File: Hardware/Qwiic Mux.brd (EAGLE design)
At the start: 40.6 x 54.6 mm, 78 parts, among them J1 SMD, J10 SMD, J11 PTH, J12 PTH, J13 PTH, J14 PTH, J2 SMD, J23 SMD, J24 SMD, J25 SMD, J26 SMD, J3 PTH, J4 PTH, J5 PTH, J6 PTH, J7 PTH, J8 SMD, J9 SMD, U2 PCA9548A, U3 3.3V/150mA, U4 2.8V/150mA

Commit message: Post design Review Changes
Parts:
- removed C10, C11, C13: 10uF, SparkFun-Capacitors:0603
- removed C12: 1.0uF, SparkFun-Capacitors:0603
- removed D1: GREEN, SparkFun-LED:LED-0603
- removed D4: BLUE, SparkFun-LED:LED-0603
- removed J11, J12, J13, J14, J3, J4, J5, J6, J7: PTH, SparkX:1X04_NO_SILK
- removed JP5: (no value), SparkFun-Jumpers:SMT-JUMPER_3_1-NC_TRACE_SILK
- removed R23, R25: 330, SparkFun-Resistors:0603
- removed U3: 3.3V/150mA, SparkFun-IC-Power:SOT23-5
- removed U4: 2.8V/150mA, SparkFun-IC-Power:SOT23-5
- added FD3, FD4: FIDUCIAL1X2, SparkFun-Aesthetics:FIDUCIAL-1X2
- added JP4: JUMPER-SMT_3_2-NC_PASTE_NO-SILK, SparkFun-Jumpers:SMT-JUMPER_3_2-NC_PASTE_NO-SILK
- added U$3: (no value), Labels-0_04:(PWR)
- added U$4: (no value), Labels-0_04:(QWIIC)
- added U$5: (no value), Labels-0_04:(I2C)
- D2: value Yellow -> RED
- R24: value 330 -> 1k
- U2: device SparkX:TSSOP28 -> SparkFun-IC-Logic:TSSOP28
- moved FD2 5.08 mm to (30.5, 1.27)
- moved H3 5.08 mm to (33.0, 52.1)
- moved H4 5.08 mm to (33.0, 2.54)
- moved J23 5.08 mm to (30.5, 10.2)
- moved J24 5.08 mm to (30.5, 20.3)
- moved J25 5.08 mm to (30.5, 30.5)
- moved J26 5.08 mm to (30.5, 40.6)
- moved JP1 2.62 mm to (20.3, 37.5)
- moved JP2 2.62 mm to (17.8, 37.5)
- moved JP3 2.62 mm to (15.2, 37.5)
- moved C2 2.55 mm to (9.14, 39.1)
- moved C3 2.55 mm to (9.14, 29.0)
- moved C4 2.55 mm to (9.14, 18.8)
- moved C5 2.55 mm to (9.14, 8.64)
- moved C6 2.55 mm to (26.4, 8.64)
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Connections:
- removed net 2.8V: C13.1, C4.1, C7.1, D1.A, J12.2, J24.2, J6.2, J9.2, R10.1, R13.1, R14.1, R9.1, U4.5
- removed net 5V: C10.1, C5.1, C6.1, D4.A, J10.2, J11.2, J23.2, J7.2, JP5.1, R11.1, R12.1, R2.1, R3.1, U3.1, U3.3
- removed net N$4: D4.C, R23.2
- removed net VIN: J2.2, J3.2, JP5.2
- new net N$2: JP4.3, R4.1
- net 3.3V: now also C4.1, C5.1, C6.1, C7.1, J10.2, J2.2, J23.2, J24.2, J9.2, JP4.2, R10.1, R11.1, R12.1, R13.1, R14.1, R2.1, R3.1, R9.1; no longer C11.1, C12.1, J13.2, J14.2, J4.2, J5.2, JP5.3, R4.1, R5.1, U3.5, U4.1, U4.3
- net GND: no longer C10.2, C11.2, C12.2, C13.2, J11.1, J12.1, J13.1, J14.1, J3.1, J4.1, J5.1, J6.1, J7.1, R23.1, R25.1, U3.2, U4.2
- net MAIN_SCL: no longer J3.4
- net MAIN_SDA: no longer J3.3
- net N$3: now also JP4.1, R5.1; no longer D1.C, R25.2
- net SCL0: no longer J4.4
- net SCL1: no longer J5.4
- net SCL2: no longer J6.4
- net SCL3: no longer J7.4
- net SCL4: no longer J11.4
- net SCL5: no longer J12.4
- net SCL6: no longer J13.4
- net SCL7: no longer J14.4
- net SDA0: no longer J4.3
- net SDA1: no longer J5.3
- net SDA2: no longer J6.3
- net SDA3: no longer J7.3
- net SDA4: no longer J11.3
- net SDA5: no longer J12.3
- net SDA6: no longer J13.3
- net SDA7: no longer J14.3
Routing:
- net 5V: track 115.1 -> 0.00 mm, vias 3 -> 0
- net 2.8V: track 105.9 -> 0.00 mm, vias 3 -> 0
- net 3.3V: track 213.8 -> 256.0 mm, vias 4 -> 6
- net VIN: track 8.46 -> 0.00 mm
- net SCL2: track 19.3 -> 13.8 mm
- net SCL3: track 25.9 -> 20.5 mm
- net SCL4: track 23.9 -> 19.8 mm
- net SCL0: track 26.4 -> 22.5 mm
- net SDA4: track 23.8 -> 20.0 mm
- net SDA2: track 16.6 -> 12.9 mm
- net SDA5: track 15.8 -> 12.3 mm
- net SCL1: track 19.8 -> 16.4 mm
- net SDA0: track 27.6 -> 24.3 mm
- net SDA7: track 31.5 -> 28.2 mm
- net SDA6: track 22.6 -> 19.3 mm
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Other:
- board size 40.6 x 54.6 mm -> 35.6 x 54.6 mm
- board text added: "I C Mux"
- board text added: "Measures in Inches"
- board text removed: "2.8V"
- board text removed: "3.3V"
- board text removed: "5V"
- board text removed: "GND"
- board text removed: "Qwiic I C Mux"
- board text removed: "SCL"
- board text removed: "SCL0"
- board text removed: "SCL1"
- board text removed: "SCL2"
- board text removed: "SCL3"
- board text removed: "SCL4"
- board text removed: "SCL5"
- board text removed: "SCL6"
- board text removed: "SCL7"
- board text removed: "SDA"
- board text removed: "SDA0"
- board text removed: "SDA1"
- board text removed: "SDA2"
- board text removed: "SDA3"
- board text removed: "SDA4"
- board text removed: "SDA5"
- board text removed: "SDA6"
- board text removed: "SDA7"
- board text removed: "VIN"
- board text removed: "VIN SEL"

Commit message: checklist changes
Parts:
- added U$10, U$21: (no value), buzzard_labels (10):44
- added U$11, U$22: (no value), buzzard_labels (10):55
- added U$12, U$6: (no value), buzzard_labels (10):00
- added U$13, U$24: (no value), buzzard_labels (10):77
- added U$14, U$26: (no value), buzzard_labels (10):#RST10
- added U$15: (no value), buzzard_labels (10):I2C_MUX8
- added U$16, U$25: (no value), buzzard_labels (11):MAIN0
- added U$17, U$23: (no value), buzzard_labels (11):61
- added U$18, U$7: (no value), buzzard_labels (10):11
- added U$19, U$8: (no value), buzzard_labels (10):22
- added U$20, U$9: (no value), buzzard_labels (10):33
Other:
- board text added: "v10"
- board text removed: "!RST"
- board text removed: "3"
- board text removed: "4"
- board text removed: "5"
- board text removed: "6"
- board text removed: "7"
- board text removed: "I C Mux"
- board text removed: "Main"
- board text removed: "v01"

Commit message: Updated Qwiic connector
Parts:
- J1, J10, J23, J24, J25, J26, J8, J9: value SMD -> (none); device SparkX:1X04_1MM_RA -> SparkFun-Connectors:1X04_1MM_RA
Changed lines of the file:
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@@
 <layer number="59" name="tCarbon" color="7" fill="1" visible="no" active="no"/>
 <layer number="60" name="bCarbon" color="7" fill="1" visible="no" active="no"/>
+<layer number="88" name="SimResults" color="9" fill="1" visible="no" active="no"/>
+<layer number="89" name="SimProbes" color="9" fill="1" visible="no" active="no"/>
 <layer number="90" name="Modules" color="5" fill="1" visible="no" active="no"/>
 <layer number="91" name="Nets" color="2" fill="1" visible="no" active="no"/>
@@
 <element name="FD1" library="SparkFun-Aesthetics" package="FIDUCIAL-1X2" value="FIDUCIAL1X2" x="5.08" y="53.34" rot="R180"/>
 <element name="FD2" library="SparkFun-Aesthetics" package="FIDUCIAL-1X2" value="FIDUCIAL1X2" x="30.48" y="1.27" rot="R180"/>
-<element name="J1" library="SparkX" package="1X04_1MM_RA" value="SMD" x="5.08011875" y="40.63921875" smashed="yes" rot="R270">
+<element name="J1" library="SparkFun-Connectors" package="1X04_1MM_RA" value="" x="5.08011875" y="40.63921875" smashed="yes" rot="R270">
 <attribute name="NAME" x="2.92111875" y="42.03621875" size="0.6096" layer="25" font="vector" ratio="20" rot="R270"/>
-</element>
-<element name="J8" library="SparkX" package="1X04_1MM_RA" value="SMD" x="5.08011875" y="30.47921875" rot="R270"/>
-<element name="J9" library="SparkX" package="1X04_1MM_RA" value="SMD" x="5.08011875" y="20.31921875" rot="R270"/>
-<element name="J10" library="SparkX" package="1X04_1MM_RA" value="SMD" x="5.08011875" y="10.15921875" rot="R270"/>
+<attribute name="PROD_ID" value="CONN-13694" x="5.08011875" y="40.63921875" size="1.778" layer="27" rot="R270" display="off"/>
+<attribute name="VALUE" value="" x="5.08011875" y="40.63921875" size="1.778" layer="27" rot="R270" display="off"/>
+</element>
+<element name="J8" library="SparkFun-Connectors" package="1X04_1MM_RA" value="" x="5.08011875" y="30.47921875" rot="R270">
+<attribute name="PROD_ID" value="CONN-13694" x="5.08011875" y="30.47921875" size="1.778" layer="27" rot="R270" display="off"/>
+<attribute name="VALUE" value="" x="5.08011875" y="30.47921875" size="1.778" layer="27" rot="R270" display="off"/>
+</element>
+<element name="J9" library="SparkFun-Connectors" package="1X04_1MM_RA" value="" x="5.08011875" y="20.31921875" rot="R270">
+<attribute name="PROD_ID" value="CONN-13694" x="5.08011875" y="20.31921875" size="1.778" layer="27" rot="R270" display="off"/>
+<attribute name="VALUE" value="" x="5.08011875" y="20.31921875" size="1.778" layer="27" rot="R270" display="off"/>
+</element>
+<element name="J10" library="SparkFun-Connectors" package="1X04_1MM_RA" value="" x="5.08011875" y="10.15921875" rot="R270">
+<attribute name="PROD_ID" value="CONN-13694" x="5.08011875" y="10.15921875" size="1.778" layer="27" rot="R270" display="off"/>
+<attribute name="VALUE" value="" x="5.08011875" y="10.15921875" size="1.778" layer="27" rot="R270" display="off"/>
+</element>
 <element name="U$1" library="SparkFun-Aesthetics" package="SFE_LOGO_NAME_FLAME_.1" value="SFE_LOGO_NAME_FLAME.1_INCH" x="11.938" y="14.732"/>
 <element name="U$2" library="SparkFun-Aesthetics" package="SFE_LOGO_NAME_FLAME_.1" value="SFE_LOGO_NAME_FLAME.1_INCH" x="23.538" y="2.223" rot="MR0"/>
@@
 <attribute name="VALUE" value="4.7k" x="7.62011875" y="10.41321875" size="0.4064" layer="27" font="vector" rot="R180"/>
 </element>
-<element name="J23" library="SparkX" package="1X04_1MM_RA" value="SMD" x="30.47921875" y="10.15988125" rot="R90"/>
-<element name="J24" library="SparkX" package="1X04_1MM_RA" value="SMD" x="30.47921875" y="20.31988125" rot="R90"/>
-<element name="J25" library="SparkX" package="1X04_1MM_RA" value="SMD" x="30.47921875" y="30.47988125" rot="R90"/>
-<element name="J26" library="SparkX" package="1X04_1MM_RA" value="SMD" x="30.47921875" y="40.63988125" rot="R90"/>
+<element name="J23" library="SparkFun-Connectors" package="1X04_1MM_RA" value="" x="30.47921875" y="10.15988125" rot="R90">
+<attribute name="PROD_ID" value="CONN-13694" x="30.47921875" y="10.15988125" size="1.778" layer="27" rot="R90" display="off"/>
+<attribute name="VALUE" value="" x="30.47921875" y="10.15988125" size="1.778" layer="27" rot="R90" display="off"/>
+</element>
+<element name="J24" library="SparkFun-Connectors" package="1X04_1MM_RA" value="" x="30.47921875" y="20.31988125" rot="R90">
+<attribute name="PROD_ID" value="CONN-13694" x="30.47921875" y="20.31988125" size="1.778" layer="27" rot="R90" display="off"/>
+<attribute name="VALUE" value="" x="30.47921875" y="20.31988125" size="1.778" layer="27" rot="R90" display="off"/>
+</element>
+<element name="J25" library="SparkFun-Connectors" package="1X04_1MM_RA" value="" x="30.47921875" y="30.47988125" rot="R90">
+<attribute name="PROD_ID" value="CONN-13694" x="30.47921875" y="30.47988125" size="1.778" layer="27" rot="R90" display="off"/>
+<attribute name="VALUE" value="" x="30.47921875" y="30.47988125" size="1.778" layer="27" rot="R90" display="off"/>
+</element>
+<element name="J26" library="SparkFun-Connectors" package="1X04_1MM_RA" value="" x="30.47921875" y="40.63988125" rot="R90">
+<attribute name="PROD_ID" value="CONN-13694" x="30.47921875" y="40.63988125" size="1.778" layer="27" rot="R90" display="off"/>
+<attribute name="VALUE" value="" x="30.47921875" y="40.63988125" size="1.778" layer="27" rot="R90" display="off"/>
+</element>
 <element name="R2" library="SparkFun-Resistors" package="0603" value="4.7k" x="26.41588125" y="10.16078125">
 <attribute name="PROD_ID" value="RES-07857" x="-19.30411875" y="20.32078125" size="1.778" layer="27" font="vector" ratio="15" display="off"/>

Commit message: Update Board
Add second "Main" Qwiic connector
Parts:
- added J3: SMD, SparkX:1X04_1MM_RA
- added U$27, U$28: (no value), buzzard_labels (11):MAIN0
- moved U$3 45.2 mm to (23.4, 47.0)
- moved D2 44.4 mm to (25.9, 48.8), turned to 0 degrees
- moved R24 42.2 mm to (25.9, 50.3), turned to 0 degrees
- moved U$2 7.62 mm to (23.5, 9.84)
- moved U$15 2.16 mm to (11.9, 14.0)
- moved U$4 1.91 mm to (14.9, 15.9)
- moved U$1 1.27 mm to (11.9, 16.0)
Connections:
- net 3.3V: now also J3.2
- net GND: now also J3.1
- net MAIN_SCL: now also J3.4
- net MAIN_SDA: now also J3.3
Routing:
- net MAIN_SDA: track 32.0 -> 55.2 mm, vias 2 -> 3
- net MAIN_SCL: track 34.5 -> 56.9 mm
- net 3.3V: track 256.0 -> 267.6 mm
- net N$1: track 2.08 -> 1.54 mm
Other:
- board text added: "v1.1"
- board text removed: "v10"

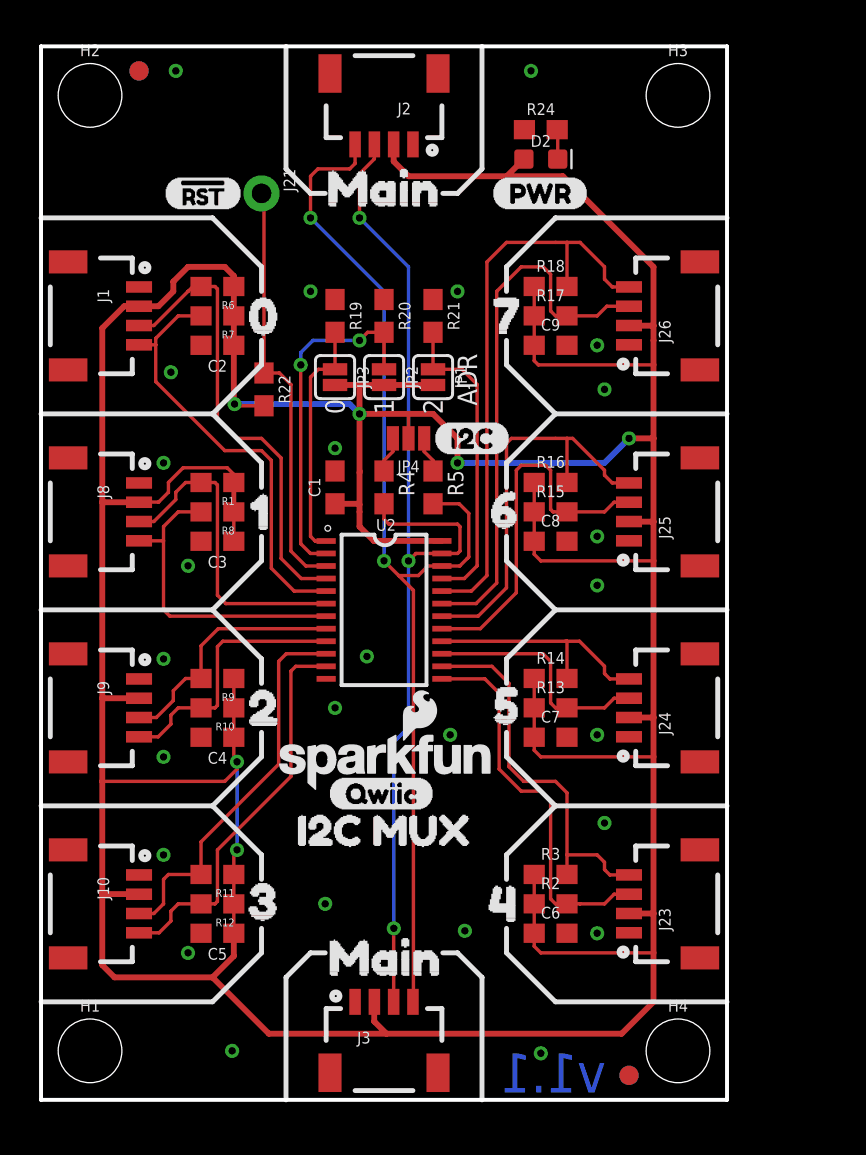
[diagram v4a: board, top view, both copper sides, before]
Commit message: Fix routing and version numbering
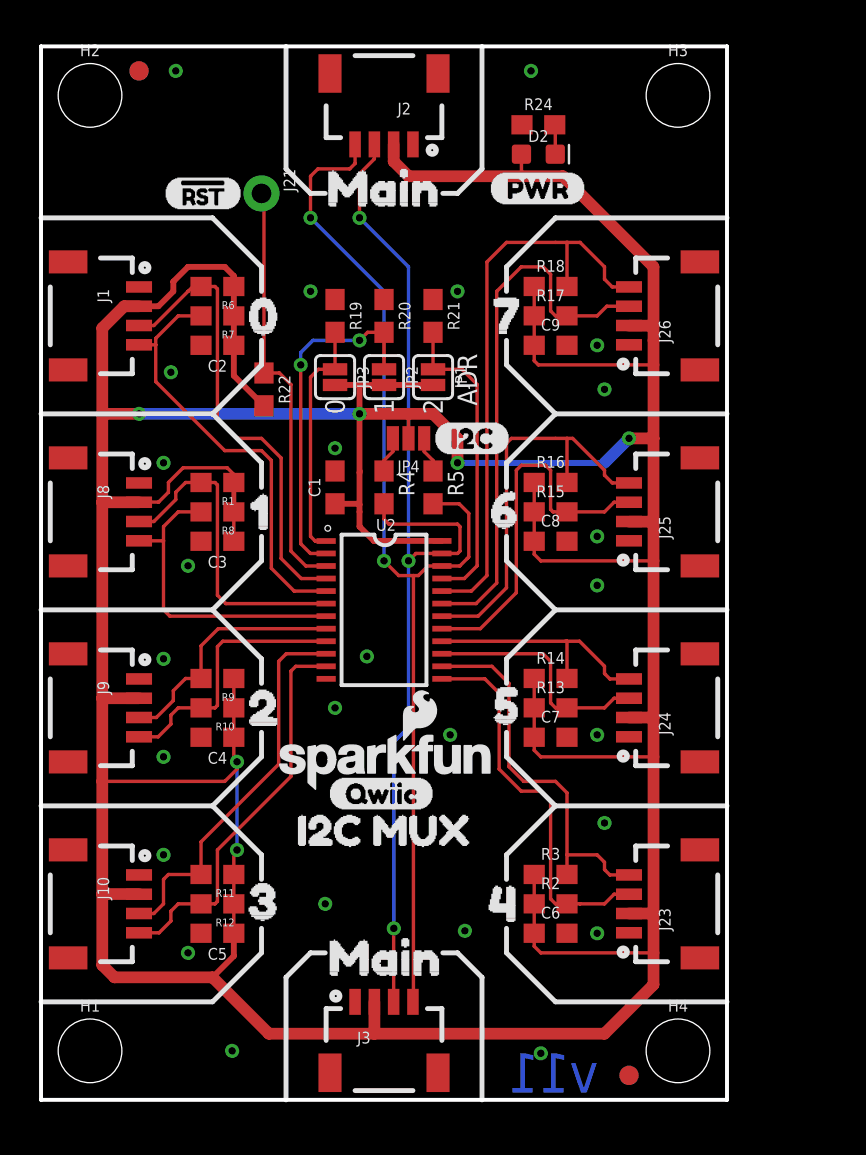
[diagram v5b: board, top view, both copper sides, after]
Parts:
- moved D2 0.28 mm to (25.8, 49.0)
- moved R24 0.28 mm to (25.8, 50.5)
- moved U$3 0.28 mm to (23.2, 47.2)
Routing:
- net 3.3V: track 267.6 -> 272.4 mm
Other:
- board text added: "v11"
- board text removed: "v1.1"
